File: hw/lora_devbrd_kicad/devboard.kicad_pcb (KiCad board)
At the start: 2 copper layers, 64.5 x 58.9 mm, 39 parts, among them J1 Conn_01x11_Male, J2 Conn_01x11_Male, J3 3.3V, J4 USB_B_Micro, J5 GND, J6 LEDS, J7 SWD, J8 Conn_01x02_Male, SW1 FSM8JSMATR, U1 rhf78-052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

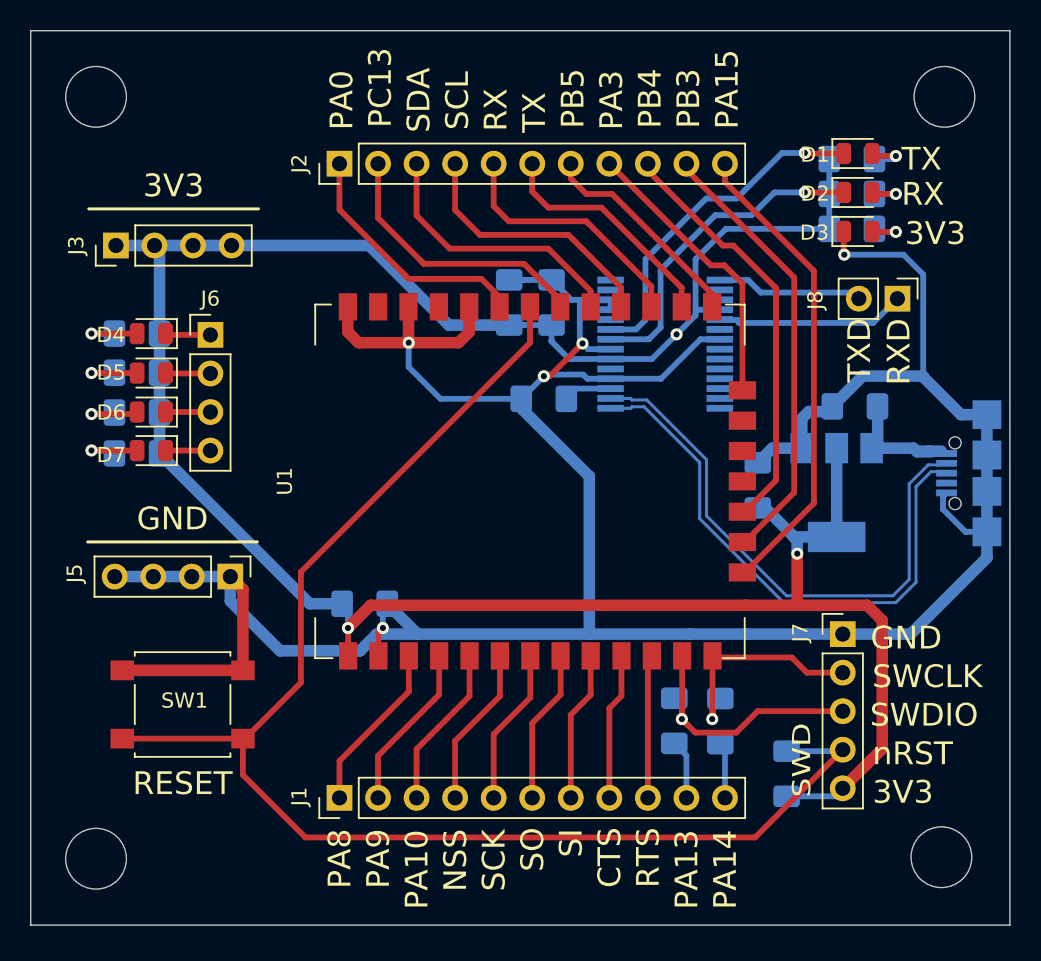
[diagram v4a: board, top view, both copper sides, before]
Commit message: WIP: [kicad] adds antennas, routing
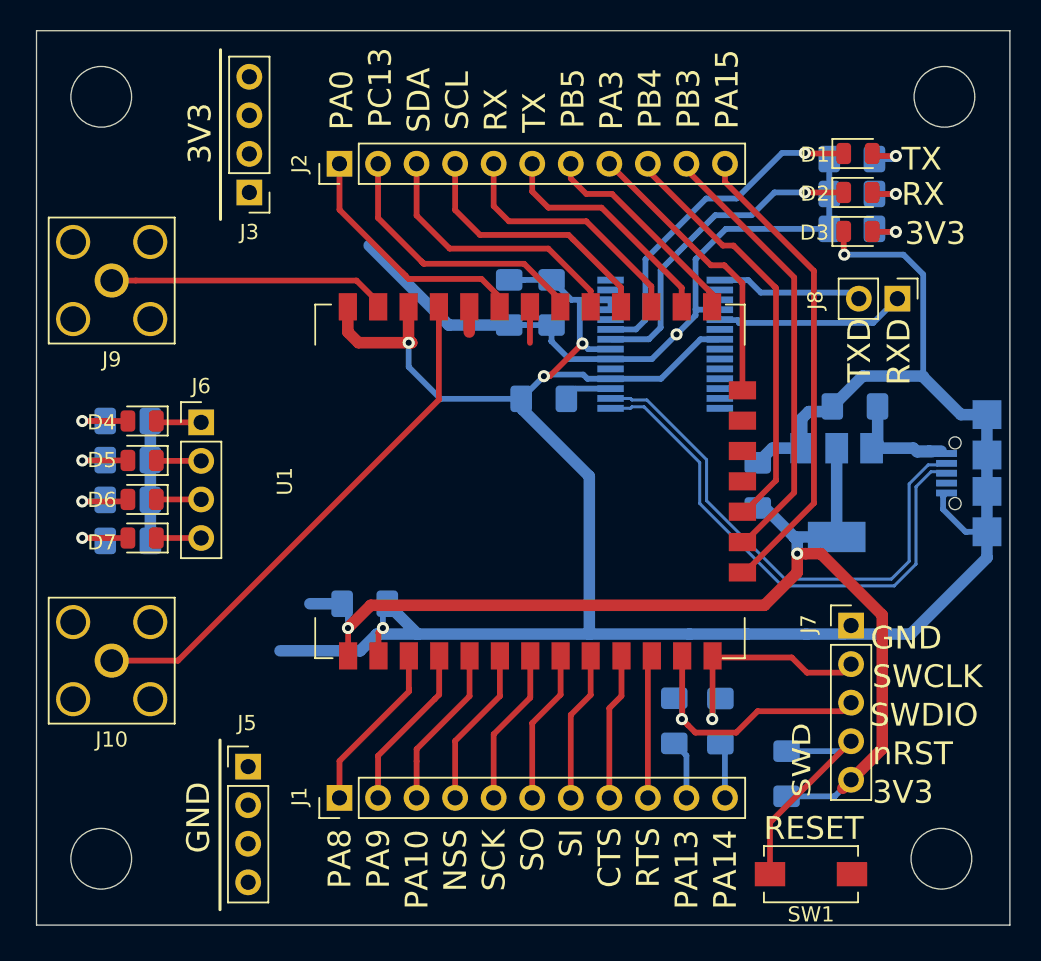
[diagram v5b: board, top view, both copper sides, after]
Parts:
- added J10: Conn_Coaxial_Power, Connector_Coaxial:SMA_Amphenol_132203-12_Horizontal, F.Cu at (121.0, 58.6)
- added J9: Conn_Coaxial_Power, Connector_Coaxial:SMA_Amphenol_132203-12_Horizontal, F.Cu at (121.0, 33.6)
- SW1: footprint Button_Switch_SMD:SW_SPST_B3S-1000 -> Button_Switch_SMD:SW_SPST_EVQPE1
- moved SW1 42.9 mm to (167.1, 72.7), turned to 180 degrees
- moved J5 12.6 mm to (130.0, 65.6), turned to 0 degrees
- moved J3 9.46 mm to (130.1, 27.8), turned to 180 degrees
- moved D4 5.79 mm to (123.0, 42.9)
- moved D7 5.79 mm to (123.0, 50.6)
- moved J6 5.79 mm to (126.9, 42.9)
- moved R5 5.79 mm to (122.1, 42.9)
- moved R6 5.79 mm to (122.1, 45.4)
- moved R7 5.79 mm to (122.1, 48.1)
- moved R8 5.79 mm to (122.1, 50.8)
- moved D5 5.79 mm to (123.0, 45.5)
- moved D6 5.79 mm to (123.0, 48.0)
- moved J7 0.79 mm to (169.7, 56.3)
- moved REF** 0.34 mm to (120.3, 21.5)
- moved REF** 0.34 mm to (120.3, 71.7)
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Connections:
- U1 pad 30: Net-(U1-Pad30) -> ANT_HF
- U1 pad 32: Net-(U1-Pad32) -> ANT_LF
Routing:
- net nRST: track 94.1 -> 16.3 mm
- net +3V3: track 165.7 -> 129.4 mm
- net ANT_HF: track 0.00 -> 34.8 mm
- net GND: track 204.4 -> 172.0 mm
- net ANT_LF: track 0.00 -> 18.5 mm
- net D-: track 37.0 -> 34.8 mm
- net D+: track 37.0 -> 34.8 mm
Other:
- board size 64.5 x 58.9 mm -> 64.1 x 58.9 mm

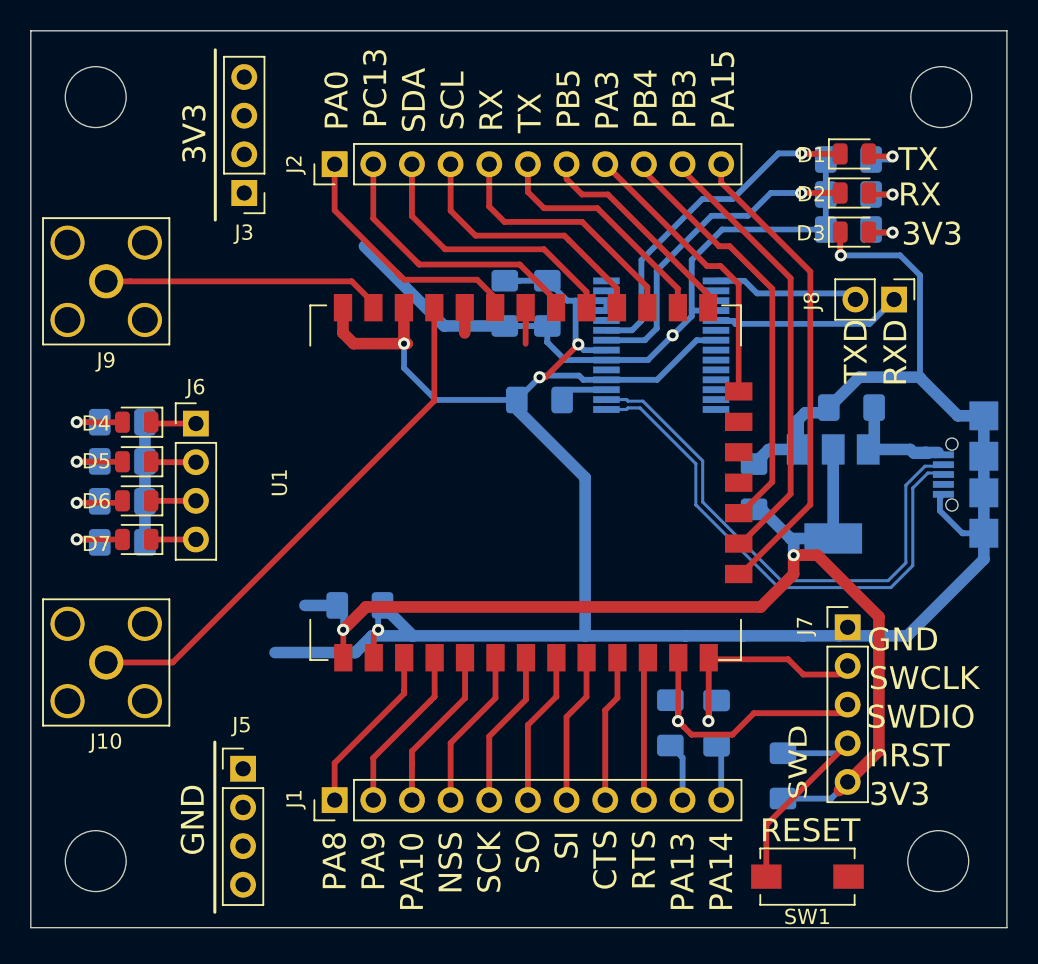
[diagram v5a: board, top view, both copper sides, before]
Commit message: WIP: [kicad] Routing, adds polygons and vias
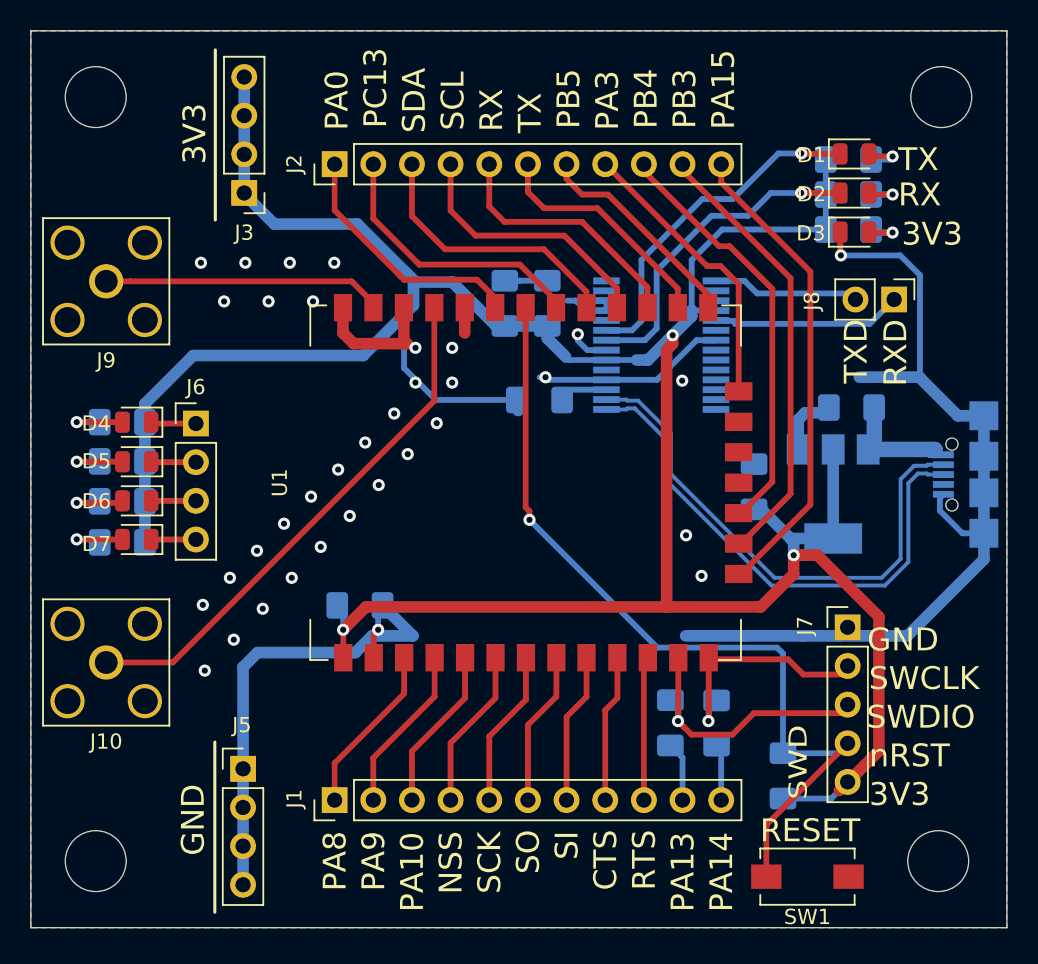
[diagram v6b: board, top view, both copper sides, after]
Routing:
- net +3V3: track 129.4 -> 186.7 mm
- net nRST: track 16.3 -> 54.8 mm, vias 0 -> 1
- net GND: track 172.0 -> 137.6 mm, vias 5 -> 35
- net D-: track 34.8 -> 35.3 mm
- added copper zone on B.Cu, net GND
- added copper zone on F.Cu, net GND

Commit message: FEAT: [kicad] DIY PCB is ready
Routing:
- net GND: track 137.6 -> 126.4 mm, vias 35 -> 33
- net SWDIO: track 17.2 -> 18.7 mm
- net D+: track 35.3 -> 34.3 mm
- net D-: track 35.3 -> 34.7 mm
